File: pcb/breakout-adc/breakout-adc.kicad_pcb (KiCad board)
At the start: 4 copper layers, 100 x 62 mm, 104 parts, among them J1 Screw_Terminal_01x04, J10 Conn_01x01_Pin, J11 Conn_01x12_Pin, J12 Conn_01x12_Pin, J13 Conn_01x01_Pin, J14 Conn_01x01_Pin, J15 FX18-120P-0.8SV20, J2 Screw_Terminal_01x02, J20 Conn_02x02_Counter_Clockwise, J21 Conn_02x04_Odd_Even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

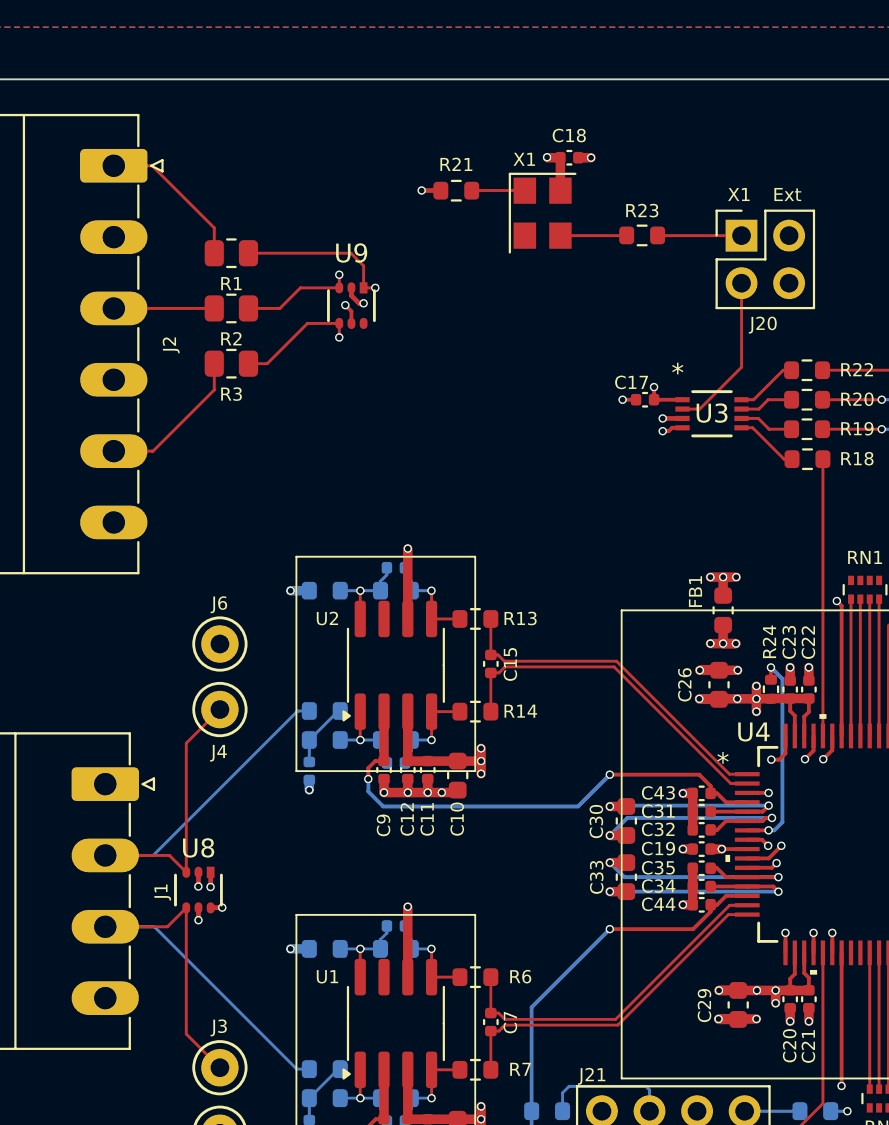
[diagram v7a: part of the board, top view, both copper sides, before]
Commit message: [adc][pcb] input silks
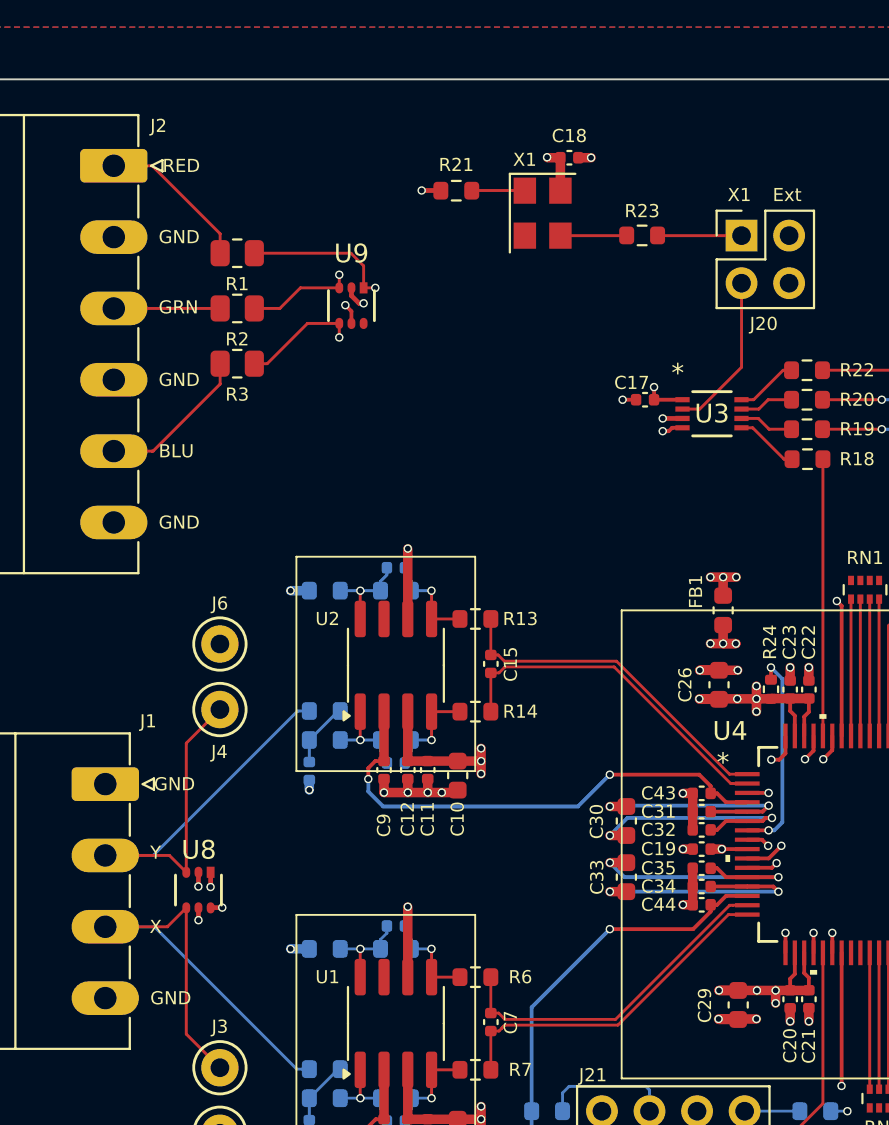
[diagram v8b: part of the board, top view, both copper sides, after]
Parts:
- moved R1 0.31 mm to (123.9, 52.8)
- moved R2 0.31 mm to (123.9, 55.8)
- moved R3 0.31 mm to (123.9, 58.7)
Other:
- board text added: "BLU"
- board text added: "GND"
- board text added: "GRN"
- board text added: "RED"
- board text added: "X"
- board text added: "Y"
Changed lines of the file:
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@@
 		(tags "ADC10DL065CIVS/NOPB ")
 		(property "Reference" "U4"
-			(at -5.456666 -5.975 0)
+			(at -6.706666 -6.05 0)
 			(unlocked yes)
 			(layer "F.SilkS")
@@
 	(footprint "Resistor_SMD:R_0805_2012Metric"
 		(layer "F.Cu")
-		(at 123.6125 52.825 180)
+		(at 123.925 52.825 180)
 		(descr "Resistor SMD 0805 (2012 Metric), square (rectangular) end terminal, IPC_7351 nominal, (Body size source: IPC-SM-782 page 72, https://www.pcb-3d.com/wordpress/wp-content/uploads/ipc-sm-782a_amendment_1_and_2.pdf), generated with kicad-footprint-generator")
 		(tags "resistor")
@@
 		(tags "phoenix_contact connector MC_01x06_G_3.81mm")
 		(property "Reference" "J2"
-			(at 9.52 -3 90)
+			(at -2.13 -2.3925 0)
 			(unlocked yes)
 			(layer "F.SilkS")
@@
 		(tags "D1213A-04S-7 ")
 		(property "Reference" "U8"
-			(at -2.215 0.004509 0)
+			(at -2.14 -0.020491 0)
 			(unlocked yes)
 			(layer "F.SilkS")
@@
 	(footprint "Resistor_SMD:R_0805_2012Metric"
 		(layer "F.Cu")
-		(at 123.6125 58.725 180)
+		(at 123.925 58.725 180)
 		(descr "Resistor SMD 0805 (2012 Metric), square (rectangular) end terminal, IPC_7351 nominal, (Body size source: IPC-SM-782 page 72, https://www.pcb-3d.com/wordpress/wp-content/uploads/ipc-sm-782a_amendment_1_and_2.pdf), generated with kicad-footprint-generator")
 		(tags "resistor")
@@
 		(tags "phoenix_contact connector MC_01x04_G_3.81mm")
 		(property "Reference" "J1"
-			(at 5.72 -3 90)
+			(at -3.355 -2.298333 0)
 			(unlocked yes)
 			(layer "F.SilkS")
@@
 	(footprint "Resistor_SMD:R_0805_2012Metric"
 		(layer "F.Cu")
-		(at 123.6125 55.775 180)
+		(at 123.925 55.775 180)
 		(descr "Resistor SMD 0805 (2012 Metric), square (rectangular) end terminal, IPC_7351 nominal, (Body size source: IPC-SM-782 page 72, https://www.pcb-3d.com/wordpress/wp-content/uploads/ipc-sm-782a_amendment_1_and_2.pdf), generated with kicad-footprint-generator")
 		(tags "resistor")
@@
 		(layer "Edge.Cuts")
 	)
+	(gr_text "GND"
+		(at 119.725 67.62 0)
+		(layer "F.SilkS")
+		(effects
+			(font
+				(size 0.7 0.7)
+				(thickness 0.1)
+			)
+			(justify left bottom)
+		)
+	)
+	(gr_text "GND"
+		(at 119.725 52.375 0)
+		(layer "F.SilkS")
+		(effects
+			(font
+				(size 0.7 0.7)
+				(thickness 0.1)
+			)
+			(justify left bottom)
+		)
+	)
 	(gr_text "Ext"
 		(at 152.52 50.125 0)
@@
 		)
 	)
+	(gr_text "BLU"
+		(at 119.725 63.81 0)
+		(layer "F.SilkS")
+		(effects
+			(font
+				(size 0.7 0.7)
+				(thickness 0.1)
+			)
+			(justify left bottom)
+		)
+	)
+	(gr_text "GND"
+		(at 119.725 60 0)
+		(layer "F.SilkS")
+		(effects
+			(font
+				(size 0.7 0.7)
+				(thickness 0.1)
+			)
+			(justify left bottom)
+		)
+	)
 	(gr_text "DCS"
 		(at 149.945 104.625 0)
@@
 		)
 	)
+	(gr_text "Y"
+		(at 119.275 85.25 0)
+		(layer "F.SilkS")
+		(effects
+			(font
+				(size 0.7 0.7)
+				(thickness 0.1)
+			)
+			(justify left bottom)
+		)
+	)
+	(gr_text "GND"
+		(at 119.476667 81.595 0)
+		(layer "F.SilkS")
+		(effects
+			(font
+				(size 0.7 0.7)
+				(thickness 0.1)
+			)
+			(justify left bottom)
+		)
+	)
 	(gr_text "OB"
 		(at 150.261667 103.675 0)
@@
 		)
 	)
+	(gr_text "GRN"
+		(at 119.725 56.125 0)
+		(layer "F.SilkS")
+		(effects
+			(font
+				(size 0.7 0.7)
+				(thickness 0.1)
+			)
+			(justify left bottom)
+		)
+	)
 	(gr_text "DCS"
 		(at 142.291667 104.625 0)
@@
 		)
 	)
+	(gr_text "GND"
+		(at 119.275 93.025 0)
+		(layer "F.SilkS")
+		(effects
+			(font
+				(size 0.7 0.7)
+				(thickness 0.1)
+			)
+			(justify left bottom)
+		)
+	)
+	(gr_text "X"
+		(at 119.241667 89.215 0)
+		(layer "F.SilkS")
+		(effects
+			(font
+				(size 0.7 0.7)
+				(thickness 0.1)
+			)
+			(justify left bottom)
+		)
+	)
 	(gr_text "wo"
 		(at 147.755 104.625 0)
@@
 		)
 	)
+	(gr_text "RED"
+		(at 119.9325 48.57 0)
+		(layer "F.SilkS")
+		(effects
+			(font
+				(size 0.7 0.7)
+				(thickness 0.1)
+			)
+			(justify left bottom)
+		)
+	)
 	(gr_text "wo"
 		(at 145.275 104.625 0)
@@
 	)
 	(segment
-		(start 131.3 54.675)
-		(end 130.675 54.675)
+		(start 130.675 54.675)
+		(end 131.3 54.675)
 		(width 0.156464)
 		(layer "F.Cu")
@@
 	)
 	(segment
-		(start 124.525 52.825)
-		(end 130 52.825)
+		(start 130.675 53.5)
+		(end 130.675 54.675)
 		(width 0.156464)
 		(layer "F.Cu")
@@
 	)
 	(segment
-		(start 130.675 53.5)
-		(end 130.675 54.675)
+		(start 130 52.825)
+		(end 130.675 53.5)
 		(width 0.156464)
 		(layer "F.Cu")
@@
 	)
 	(segment
-		(start 130 52.825)
-		(end 130.675 53.5)
+		(start 124.8375 52.825)
+		(end 130 52.825)
 		(width 0.156464)
 		(layer "F.Cu")
@@
 	)
 	(segment
-		(start 126.2 55.775)
-		(end 127.3 54.675)
+		(start 129.375 54.675)
+		(end 129.375 53.975)
 		(width 0.156464)
 		(layer "F.Cu")
@@
 	)
 	(segment
-		(start 124.525 55.775)
-		(end 126.2 55.775)
+		(start 127.3 54.675)
+		(end 129.375 54.675)
 		(width 0.156464)
 		(layer "F.Cu")
@@
 	)
 	(segment
-		(start 129.375 54.675)
-		(end 129.375 53.975)
+		(start 126.2 55.775)
+		(end 127.3 54.675)
 		(width 0.156464)
 		(layer "F.Cu")
@@
 	)
 	(segment
-		(start 127.3 54.675)
-		(end 129.375 54.675)
+		(start 124.8375 55.775)
+		(end 126.2 55.775)
 		(width 0.156464)
 		(layer "F.Cu")
@@
 	)
 	(segment
-		(start 124.525 58.725)
-		(end 125.525 58.725)
+		(start 129.375 56.575)
+		(end 129.375 57.325)
 		(width 0.156464)
 		(layer "F.Cu")
@@
 	)
 	(segment
-		(start 129.375 57.325)
-		(end 129.375 56.575)
+		(start 125.525 58.725)
+		(end 127.675 56.575)
 		(width 0.156464)
 		(layer "F.Cu")
@@
 	)
 	(segment
-		(start 127.675 56.575)
-		(end 129.375 56.575)
+		(start 124.8375 58.725)
+		(end 125.525 58.725)
 		(width 0.156464)
 		(layer "F.Cu")
@@
 	)
 	(segment
-		(start 125.525 58.725)
-		(end 127.675 56.575)
+		(start 127.675 56.575)
+		(end 129.375 56.575)
 		(width 0.156464)
 		(layer "F.Cu")
@@
 	(segment
 		(start 117.3325 55.775)
-		(end 122.7 55.775)
+		(end 123.0125 55.775)
 		(width 0.156464)
 		(layer "F.Cu")
@@
 	)
 	(segment
-		(start 119.38 48.155)
-		(end 122.7 51.475)
+		(start 117.3325 48.155)
+		(end 119.38 48.155)
 		(width 0.156464)
 		(layer "F.Cu")
@@
 	)
 	(segment
-		(start 122.7 51.475)
-		(end 122.7 52.825)
+		(start 123.0125 51.7875)
+		(end 123.0125 52.825)
 		(width 0.156464)
 		(layer "F.Cu")
@@
 	)
 	(segment
-		(start 117.3325 48.155)
-		(end 119.38 48.155)
+		(start 119.38 48.155)
+		(end 123.0125 51.7875)
 		(width 0.156464)
 		(layer "F.Cu")
@@
 	)
 	(segment
-		(start 117.3325 63.395)
-		(end 119.37 63.395)
+		(start 123.0125 59.8125)
+		(end 123.0125 58.725)
 		(width 0.156464)
 		(layer "F.Cu")
@@
 	)
 	(segment
-		(start 122.7 60.125)
-		(end 122.7 58.725)
+		(start 119.43 63.395)
+		(end 123.0125 59.8125)
 		(width 0.156464)
 		(layer "F.Cu")
@@
 	)
 	(segment
-		(start 119.37 63.395)
-		(end 119.4 63.425)
+		(start 117.3325 63.395)
+		(end 119.37 63.395)
 		(width 0.156464)
 		(layer "F.Cu")
@@
 	)
 	(segment
-		(start 119.4 63.425)
-		(end 122.7 60.125)
+		(start 119.37 63.395)
+		(end 119.43 63.395)
 		(width 0.156464)
 		(layer "F.Cu")
